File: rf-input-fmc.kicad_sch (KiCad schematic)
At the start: 2 parts, among them J1 MMCX, J2 MMCX

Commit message: Updated BOM of all parts
Updated BOM of all parts
-added supplier & supplier part number to all parts
- fixed many issues with part including:R5-R8,C34,C35,C24, R10-R15

Changed filter C36&C37 to 15nF (keep COG & 0603, but changes filter cutoff to 3.8kHz|was 12kHz)
Changed bulk Caps to 22uF (was 47uF) to get a Cap with enough voltage headroom at 12V while 0805
Changed C31 to be a bulk 10uF cap
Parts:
- J1, J2: Supplier (none) -> Digikey; Supplier Part Number (none) -> SAM10617-ND
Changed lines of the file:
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@@
+			)
+		)
+		(property "Supplier" "Digikey"
+			(at 50.8 85.09 0)
+			(effects
+				(font
+					(size 1.27 1.27)
+				)
+				(hide yes)
+			)
+		)
+		(property "Supplier Part Number" "SAM10617-ND"
+			(at 50.8 85.09 0)
+			(effects
+				(font
+					(size 1.27 1.27)
+				)
+				(hide yes)
 			)
 		)
@@
 			(at 49.53 45.72 0)
 			(effects
+				(font
+					(size 1.27 1.27)
+				)
+				(hide yes)
+			)
+		)
+		(property "Supplier" "Digikey"
+			(at 49.53 45.72 0)
+			(effects
+				(font
+					(size 1.27 1.27)
+				)
+				(hide yes)
+			)
+		)
+		(property "Supplier Part Number" "SAM10617-ND"
+			(at 49.53 45.72 0)
+			(effects

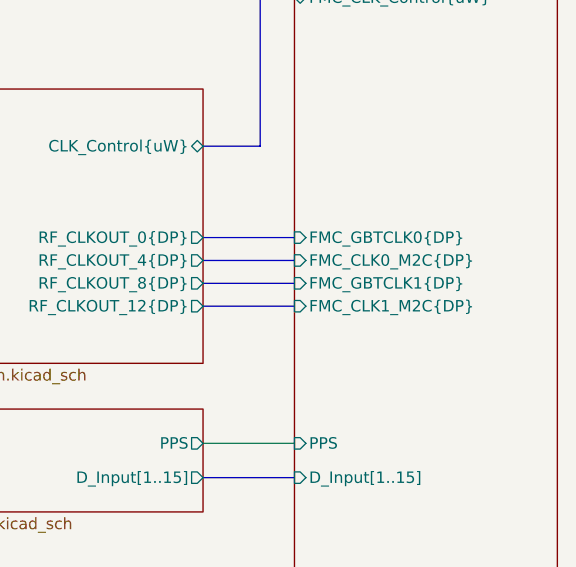
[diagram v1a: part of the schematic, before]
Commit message: Finished Board Layout
Schematic Changes
- Removed some testpoints
- Fixed Lib issues
- moved around FMC pinout

Layout
- routed all traces
- routed RF traces using Controlled Impedance in mind
- ERC/DRC free
- All silkscreen is arranged

Still to do
- finish net-classes for controlled traces
- create arc traces for diff CLK lines
- small tweaks to improve RF performance
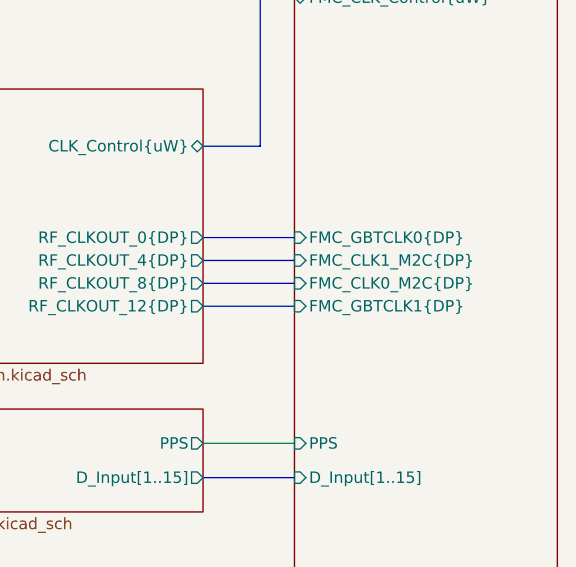
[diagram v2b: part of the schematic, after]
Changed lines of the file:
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@@
 		)
 		(pin "FMC_CLK0_M2C{DP}" input
-			(at 176.53 100.33 180)
+			(at 176.53 102.87 180)
 			(effects
 				(font
@@
 		)
 		(pin "FMC_CLK1_M2C{DP}" input
-			(at 176.53 105.41 180)
+			(at 176.53 100.33 180)
 			(effects
 				(font
@@
 		)
 		(pin "FMC_GBTCLK1{DP}" input
-			(at 176.53 102.87 180)
+			(at 176.53 105.41 180)
 			(effects
 				(font

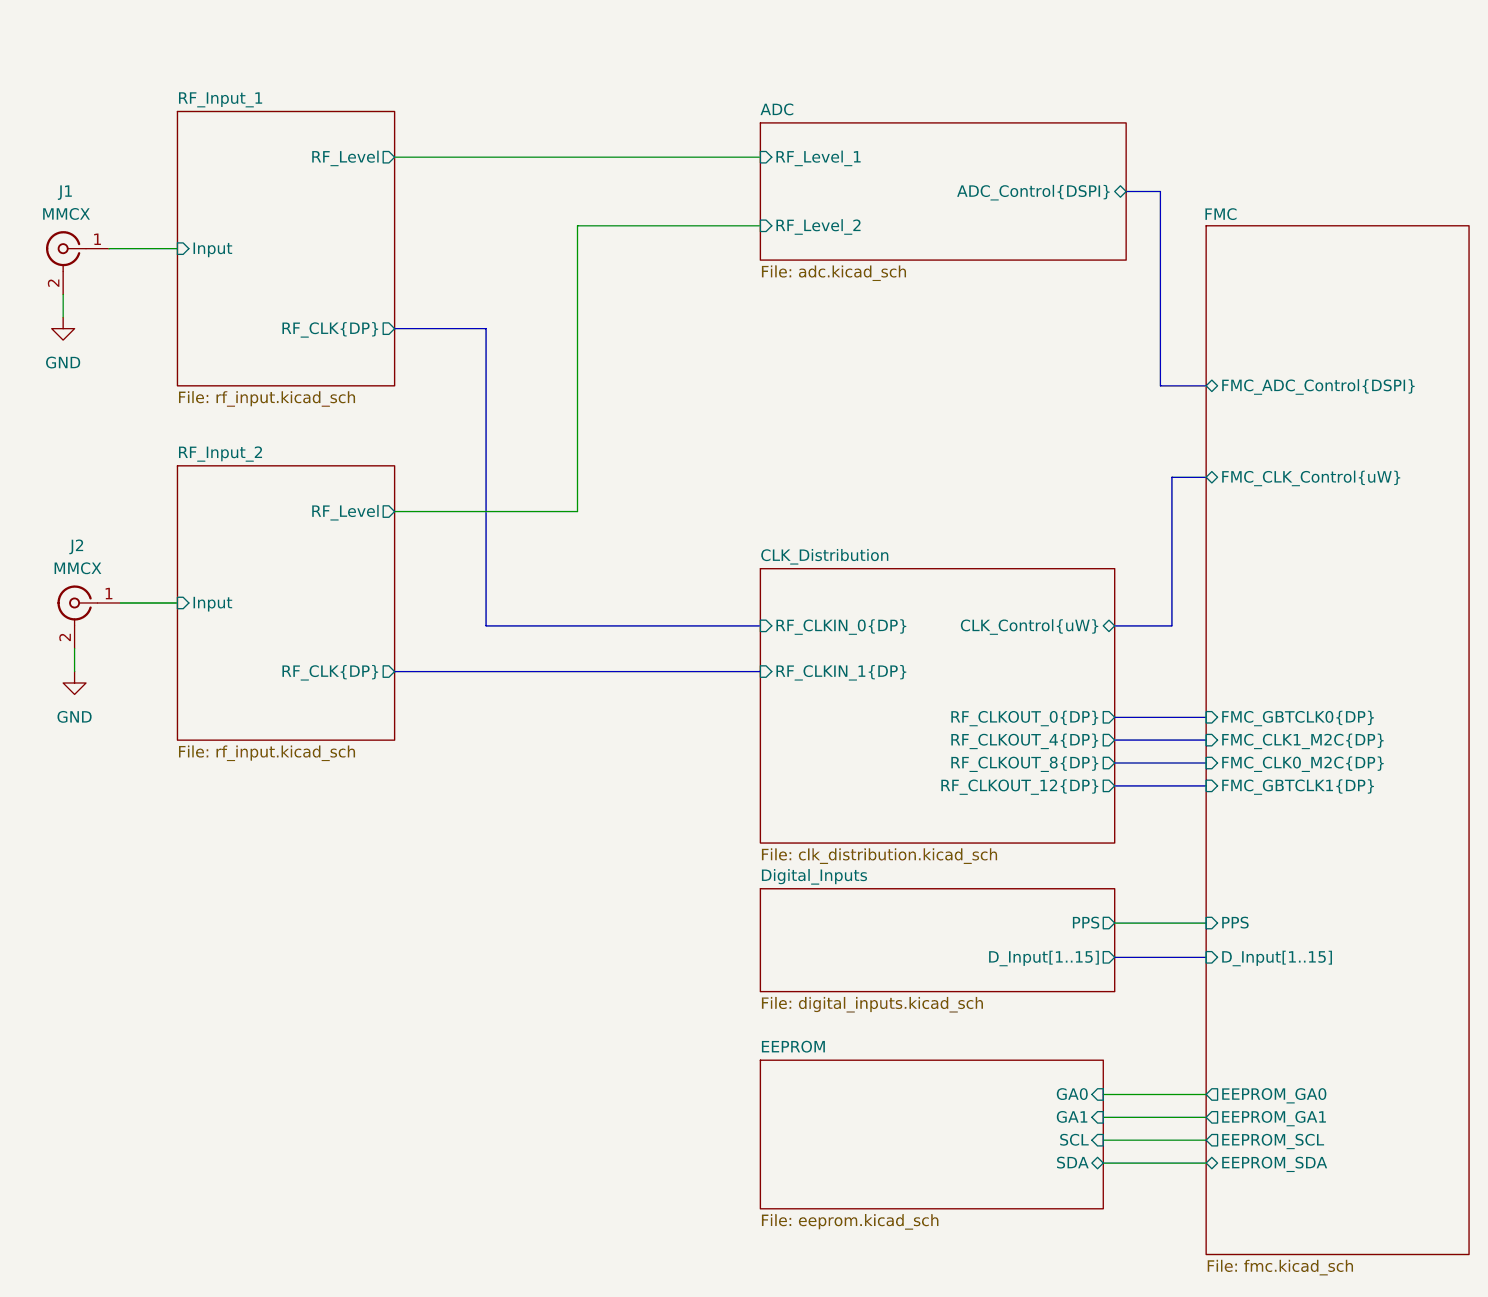
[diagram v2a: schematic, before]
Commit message: Final Draft for prototype run
- Updated CLK mapping to FMC
	 - Now Output 12 goes to M2C CLK instead of a GBT CLK
	 - Outputs 0, 4, 8 have moved
	 - all CLK now have polarity swapped at the FMC pin
		 - CLK signals maintain normal polarity through the CLK distribution chip but are now ALL swapped between the CLK Distribution IC output and the FMC pins
	- Added a monitor output on Output13 (J20)
- Moved decoupling caps to bottom of LCB in many places
- Standardized the area to the right of the FMC to use as a future template
- Moved board specific test points and function to the left
- Added an additional bypass cap on U8
- Tied the front two mounting hole (H3 &H4) to GND
- changed H2 to be a slotted hole
	- This allows for mounting in the FMC slot on Marble where to the mounting hole is shifted by ~4mil
- Add Serial Number area and Board title
- Cleaned up all silkscreen and Fab layers
- Changed J1 & J2 to SMA
	- Added 3d model (from manufacture) to footprint
-  Moved many of the major layout blocks to allow for other changes in this commit
- Added power planes for many major and minor distributed power rails
- pulled back power planes from input connectors
- Fixed all ERC & DRC errors/warnings
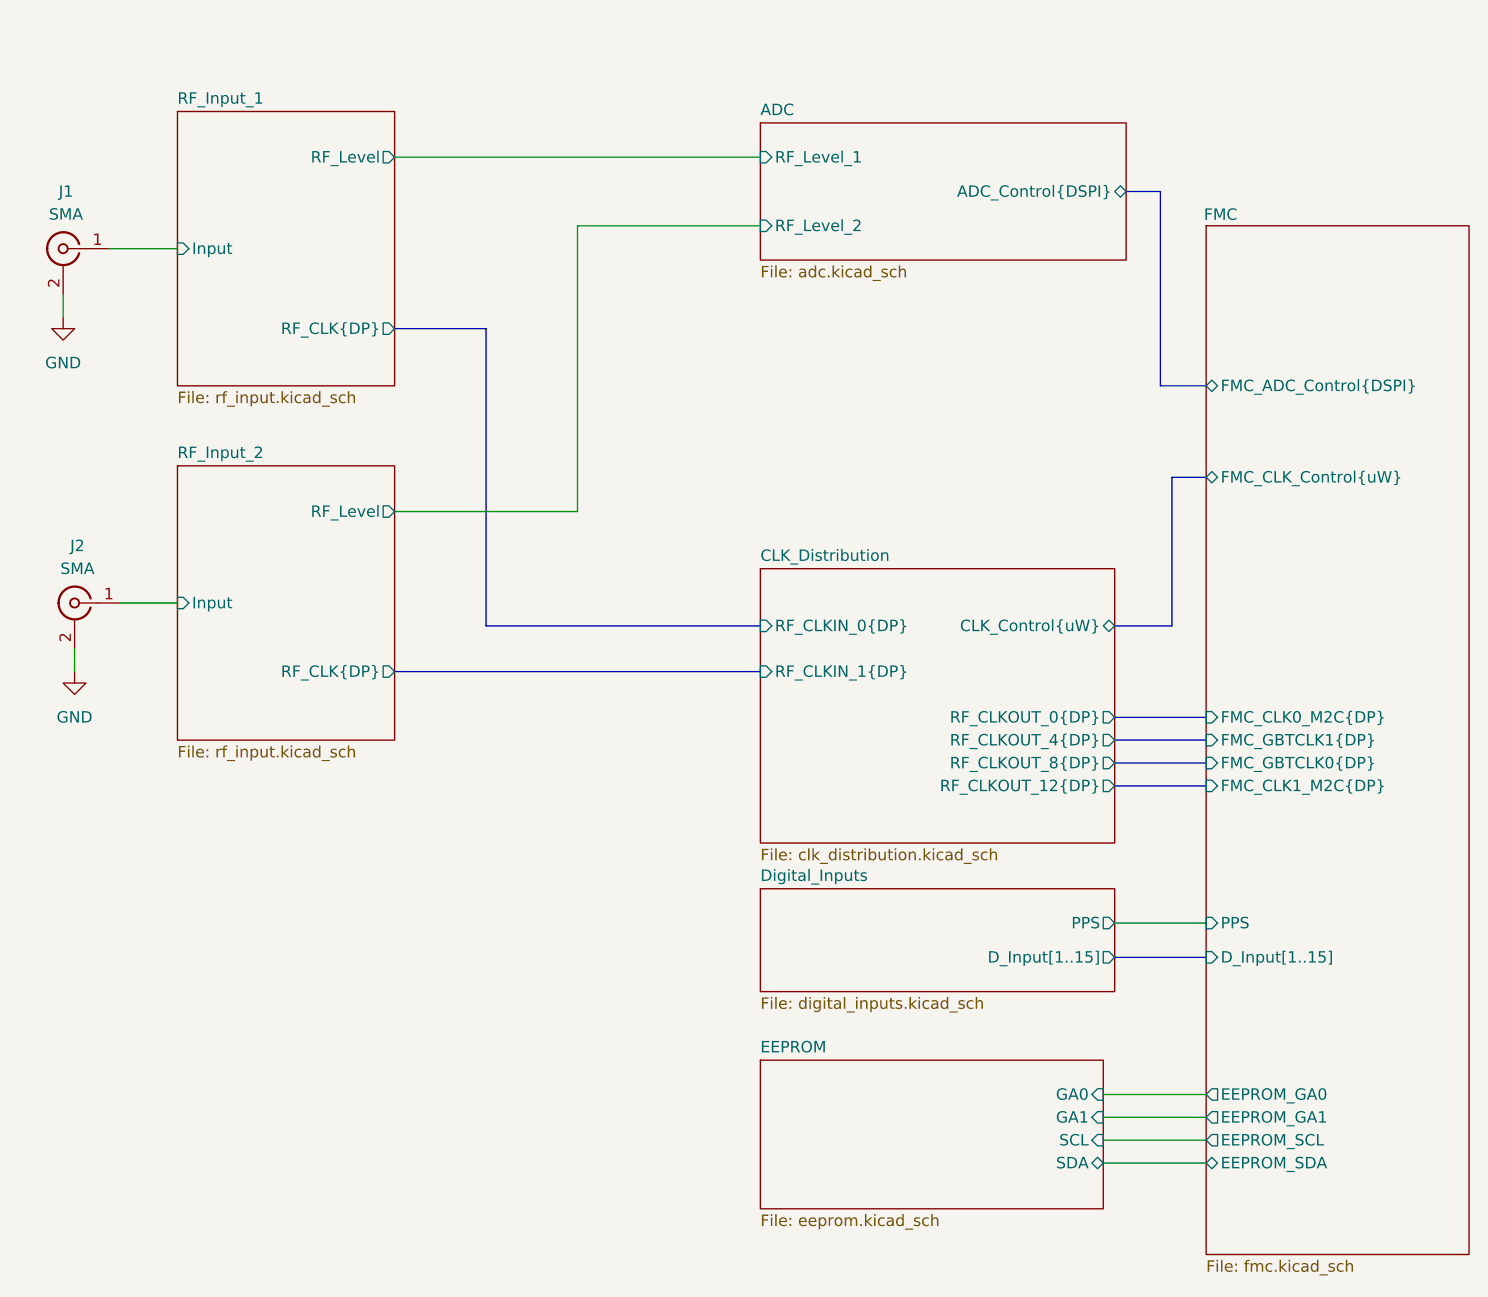
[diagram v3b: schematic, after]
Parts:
- J1, J2: value MMCX -> SMA; footprint Connector_Coaxial:MMCX_Molex_73415-1471_Vertical -> rf-input-fmc:SMA_Amphenol_901-144_Vertical; MPN MMCX-J-P-H-ST-TH1 -> 901-144-8RFX; Manufacturer Samtec Inc. -> Amphenol RF; Supplier Part Number SAM10617-ND -> ARFX1231-ND

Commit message: Prototype Production Ready
- Removed Supplier and Supplier Part Numbers for project
- Changed Kibot to not out Supplier and Supplier Part Numbers for project
- Changed a few ignored ERC/DRC testing to warnings, and found no additional issues
- project is ready for production
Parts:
- J1, J2: Supplier Digikey -> (none); Supplier Part Number ARFX1231-ND -> (none)
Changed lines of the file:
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@@
-			)
-		)
-		(property "Supplier" "Digikey"
-			(at 49.53 45.72 0)
-			(effects
-				(font
-					(size 1.27 1.27)
-				)
-				(hide yes)
-			)
-		)
-		(property "Supplier Part Number" "ARFX1231-ND"
-			(at 49.53 45.72 0)
-			(effects
-				(font
-					(size 1.27 1.27)
-				)
-				(hide yes)
 			)
 		)
@@
 			(at 50.8 85.09 0)
 			(effects
-				(font
-					(size 1.27 1.27)
-				)
-				(hide yes)
-			)
-		)
-		(property "Supplier" "Digikey"
-			(at 50.8 85.09 0)
-			(effects
-				(font
-					(size 1.27 1.27)
-				)
-				(hide yes)
-			)
-		)
-		(property "Supplier Part Number" "ARFX1231-ND"
-			(at 50.8 85.09 0)
-			(effects
